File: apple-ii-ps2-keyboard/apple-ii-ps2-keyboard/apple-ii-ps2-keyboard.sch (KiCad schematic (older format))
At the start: 26 parts, among them J1 PS/2, J2 apple-ii, J3 SHIFT_KEY, J4 EXP, J5 EXP_PWR

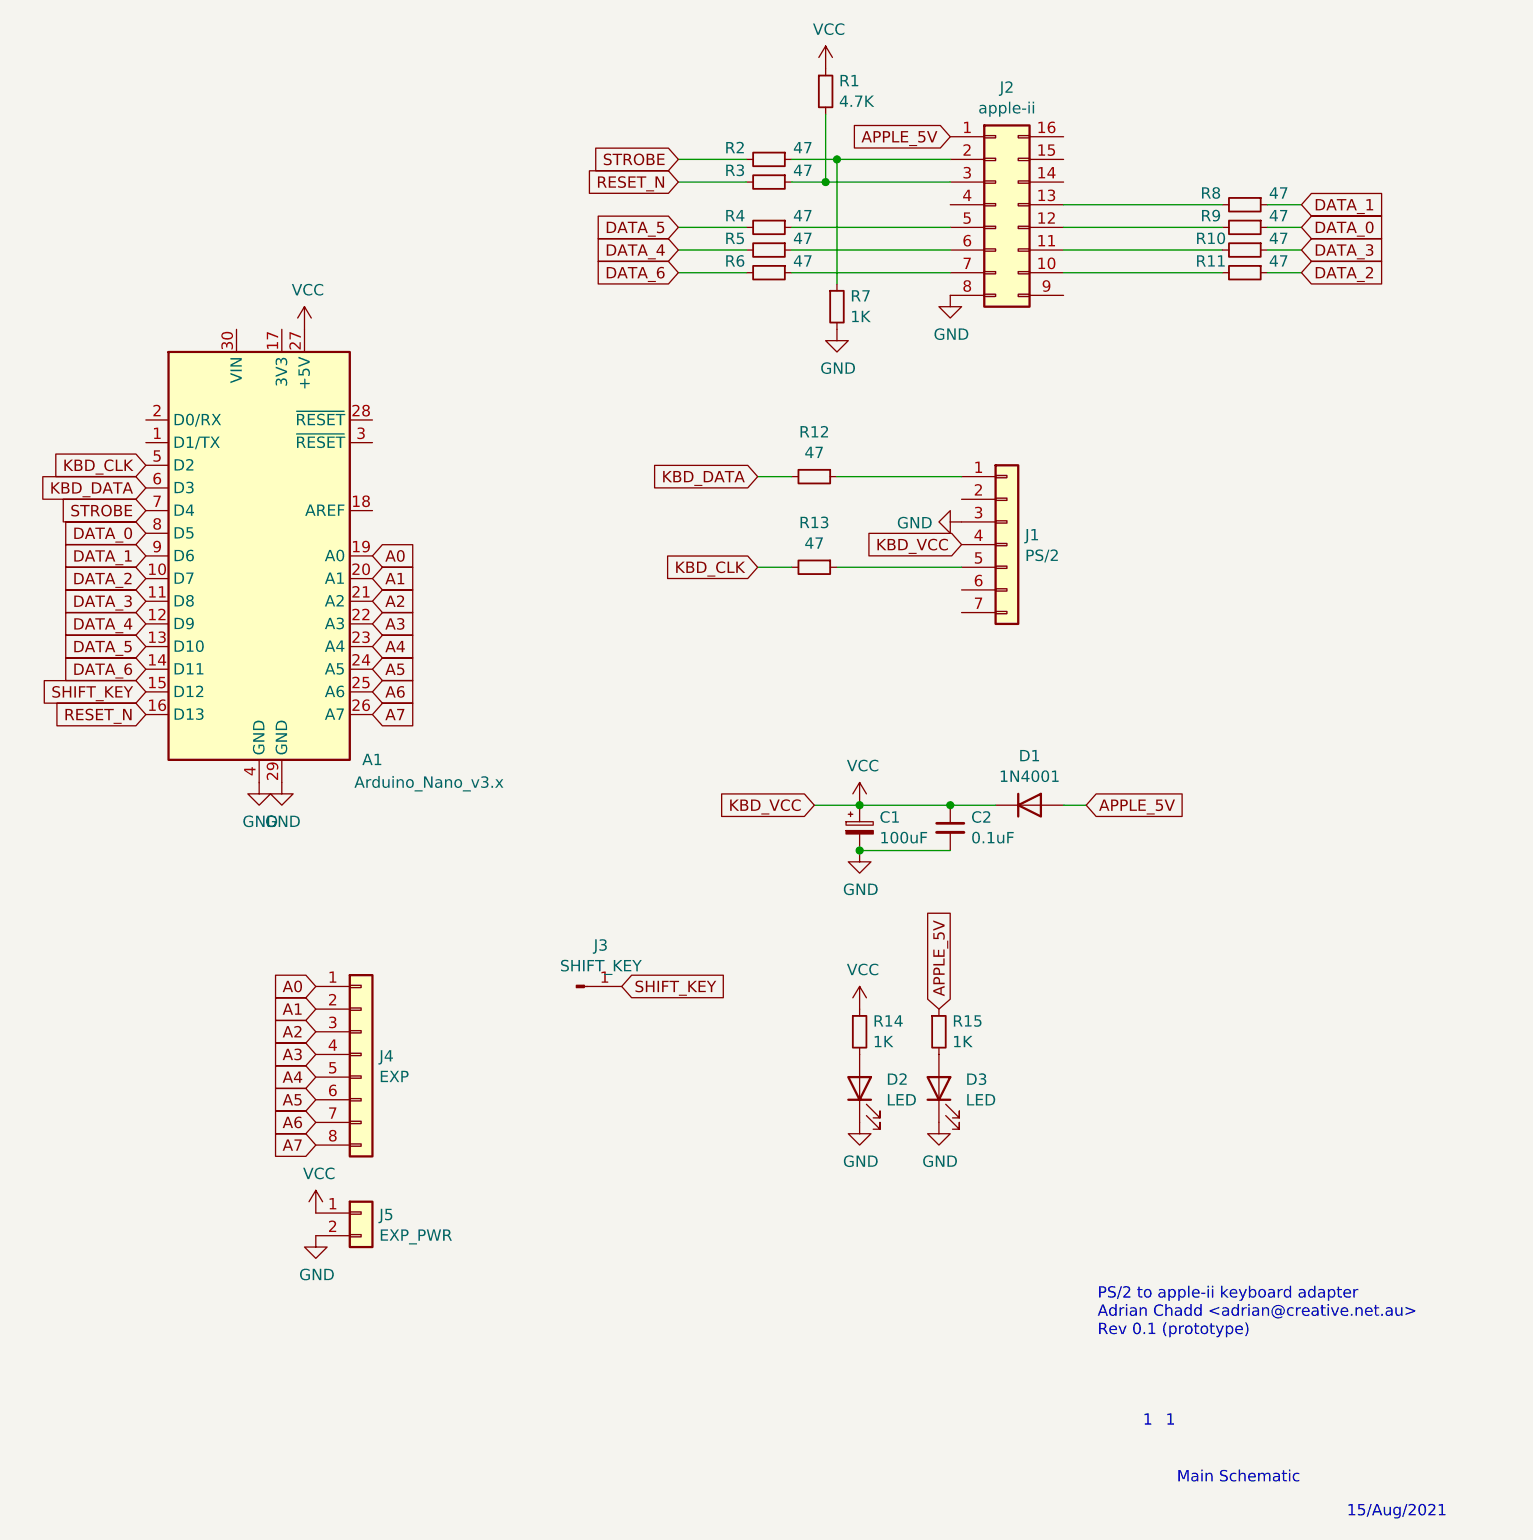
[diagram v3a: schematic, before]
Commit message: * add uart connector * add pin 7 on the ps/2 connector as a ground, for shield
ok, this may be the thing I ship!
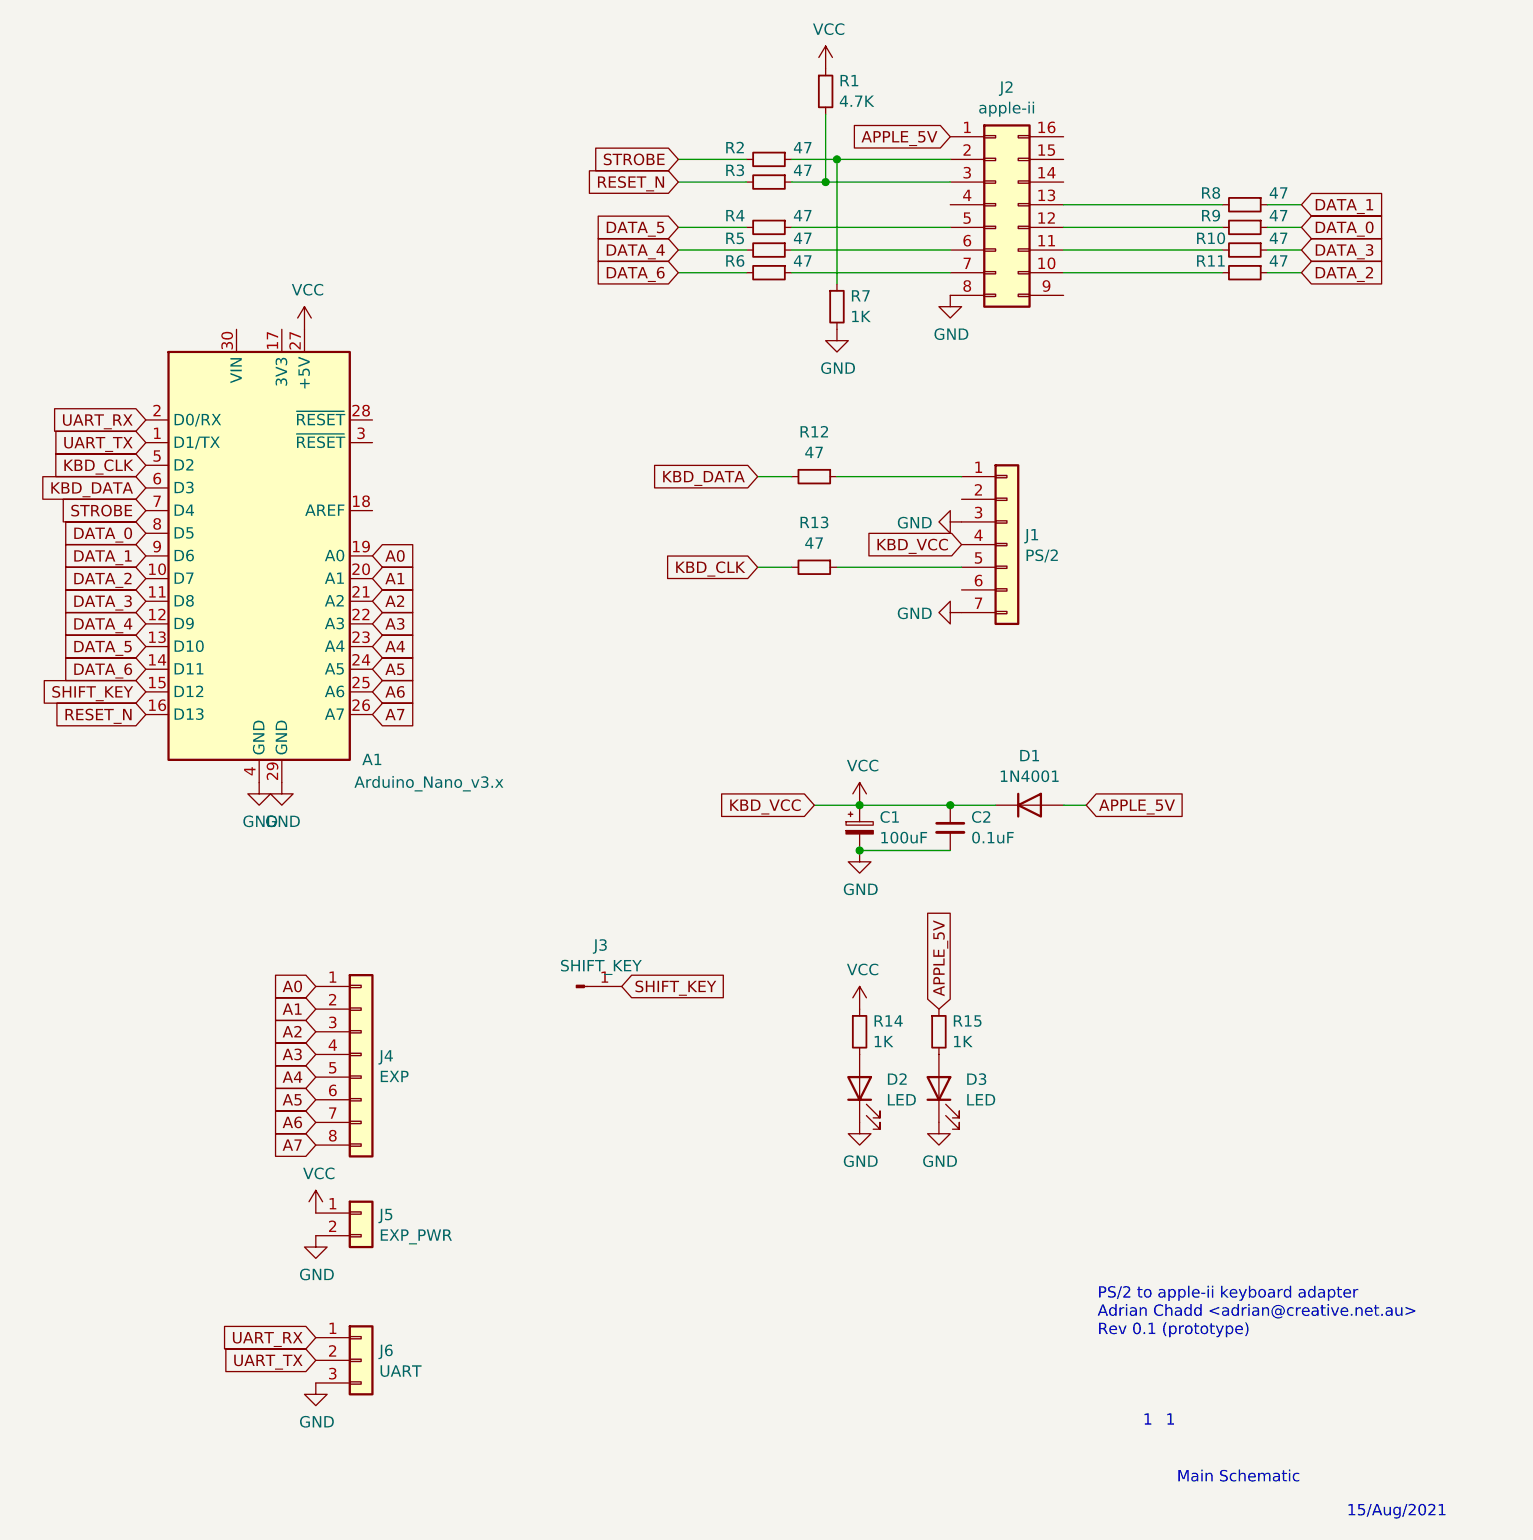
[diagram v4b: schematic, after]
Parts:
- added J6: UART, Connector_PinHeader_2.54mm:PinHeader_1x03_P2.54mm_Vertical, symbol Connector_Generic:Conn_01x03
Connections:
- net GND: now also J1.7 (Pin_7), J6.3 (Pin_3)
- net UART_TX: now reaches A1.1 (D1/TX)
- net UART_TX: now also J6.2 (Pin_2)
- net UART_RX: now reaches A1.2 (D0/RX)
- net UART_RX: now also J6.1 (Pin_1)
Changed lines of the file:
@@
 Text GLabel 3900 4100 2    50   Input ~ 0
 A7
+Text GLabel 2900 2900 0    50   Input ~ 0
+UART_TX
+Text GLabel 2900 2800 0    50   Input ~ 0
+UART_RX
+$Comp
+L Connector_Generic:Conn_01x03 J6
+U 1 1 61285525
+P 3850 6950
+F 0 "J6" H 3930 6992 50  0000 L CNN
+F 1 "UART" H 3930 6901 50  0000 L CNN
+F 2 "Connector_PinHeader_2.54mm:PinHeader_1x03_P2.54mm_Vertical" H 3850 6950 50  0001 C CNN
+F 3 "~" H 3850 6950 50  0001 C CNN
+	1    3850 6950
+	1    0    0    -1
+$EndComp
+$Comp
+L power:GND #PWR0106
+U 1 1 61288445
+P 3650 7050
+F 0 "#PWR0106" H 3650 6800 50  0001 C CNN
+F 1 "GND" H 3655 6877 50  0000 C CNN
+F 2 "" H 3650 7050 50  0001 C CNN
+F 3 "" H 3650 7050 50  0001 C CNN
+	1    3650 7050
+	1    0    0    -1
+$EndComp
+Text GLabel 3650 6850 0    50   Input ~ 0
+UART_RX
+Text GLabel 3650 6950 0    50   Input ~ 0
+UART_TX
+$Comp
+L power:GND #PWR?
+U 1 1 6129DDBB
+P 6500 3650
+F 0 "#PWR?" H 6500 3400 50  0001 C CNN
+F 1 "GND" V 6505 3522 50  0000 R CNN
+F 2 "" H 6500 3650 50  0001 C CNN
+F 3 "" H 6500 3650 50  0001 C CNN
+	1    6500 3650
+	0    1    1    0
+$EndComp
 $EndSCHEMATC
